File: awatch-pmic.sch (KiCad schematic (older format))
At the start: 14 parts

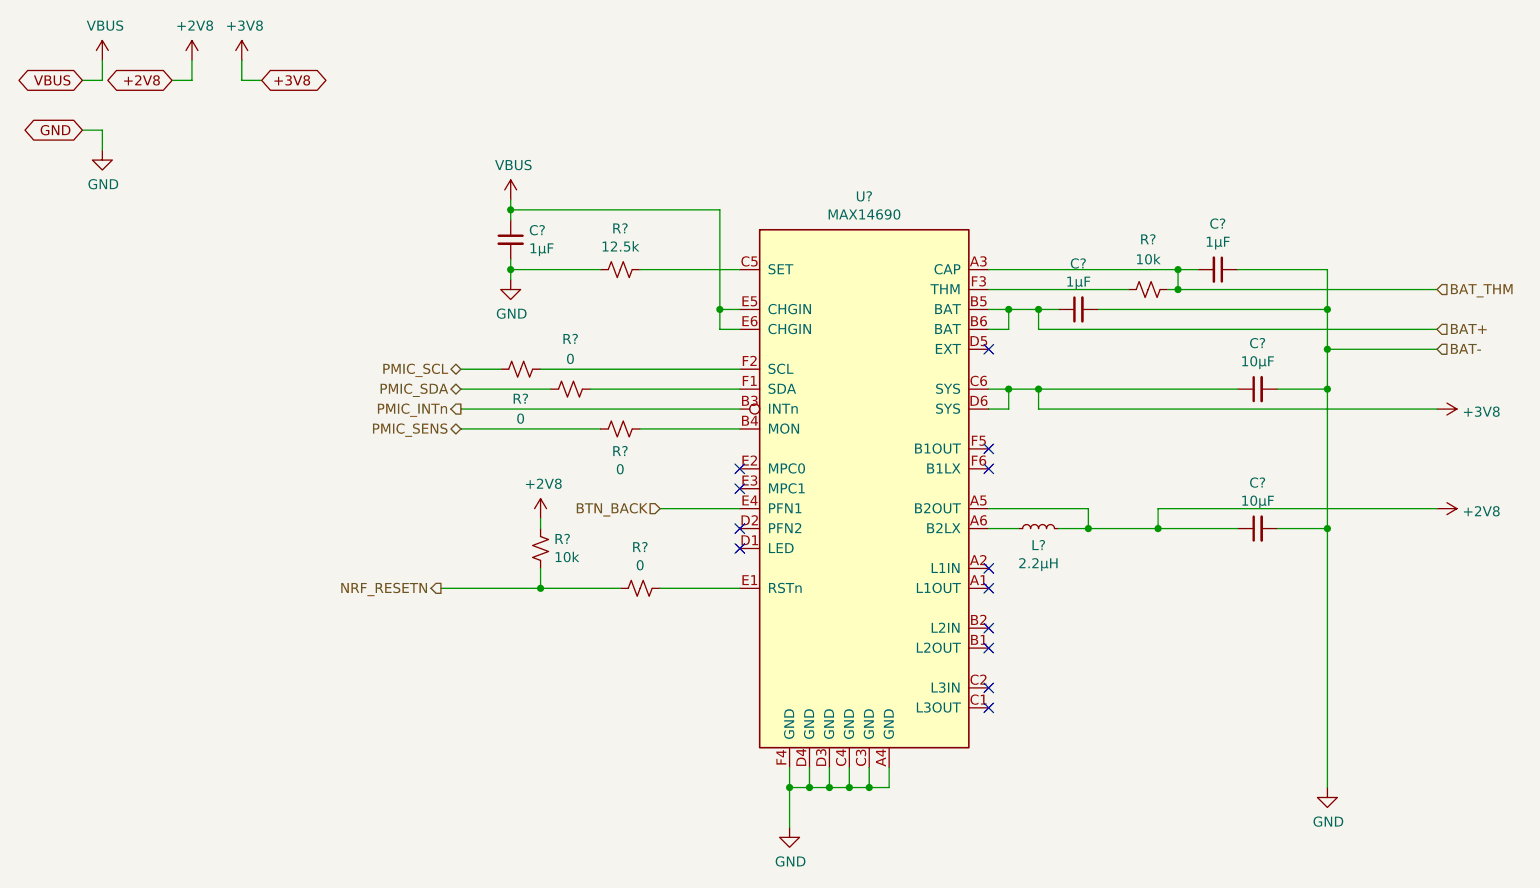
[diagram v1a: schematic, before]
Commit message: Add display.  Add +3.3V LDO for backlight.
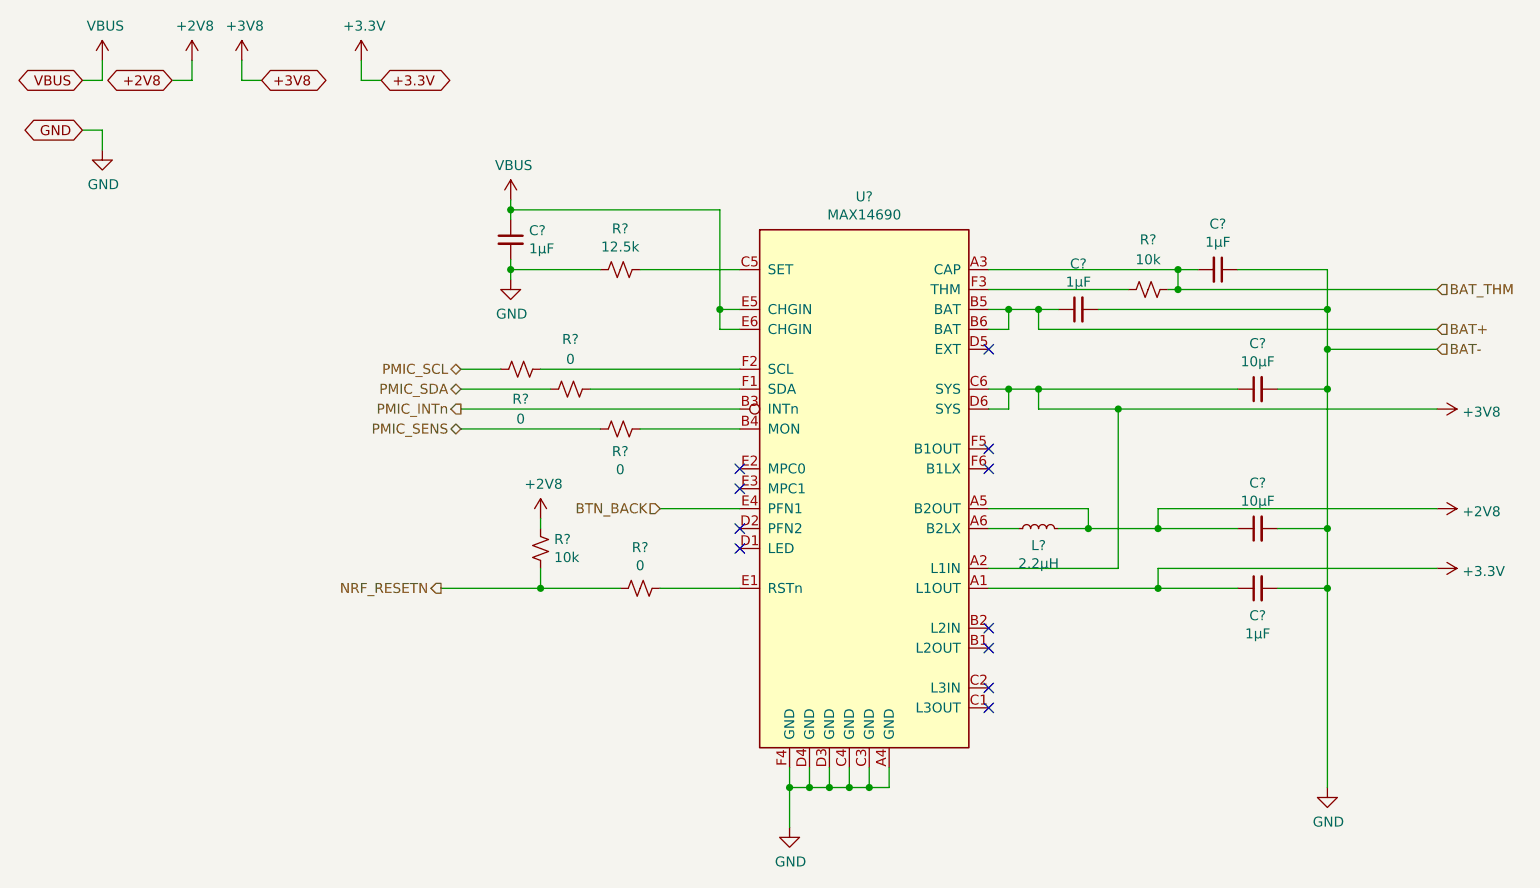
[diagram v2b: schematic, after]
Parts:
- added C?: 1µF, symbol Device:C_Small
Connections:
- net +3V8: now also U?.A2 (L1IN)
- net GND: now also C?.2
- net +3V3: now reaches U?.A1 (L1OUT)
- net +3V3: now also C?.1
- no-connect marks 13 -> 11
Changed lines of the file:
@@
 $Descr A4 11693 8268
 encoding utf-8
-Sheet 3 6
+Sheet 3 7
 Title "AWatch2"
 Date ""
@@
 	6100 2800 6100 2900
 Wire Wire Line
-	6100 2900 8100 2900
+	6100 2900 6500 2900
 Connection ~ 6100 2800
 Wire Wire Line
@@
 Connection ~ 6350 3500
 Wire Wire Line
-	6350 3500 6700 3500
-Wire Wire Line
 	6700 3500 6700 3400
 Wire Wire Line
@@
 	1    0    0    -1
 $EndComp
-NoConn ~ 5850 3700
-NoConn ~ 5850 3800
 NoConn ~ 5850 4000
 NoConn ~ 5850 4100
@@
 Connection ~ 7550 2800
 Wire Wire Line
-	7550 3500 7550 4800
+	7550 3500 7550 3800
 $Comp
 L awatch-parts:MAX14690 U?
@@
 Wire Wire Line
 	3600 3800 3100 3800
+Wire Wire Line
+	6500 3700 5850 3700
+$Comp
+L Device:C_Small C?
+U 1 1 5C4627BE
+P 7200 3800
+F 0 "C?" V 7063 3800 50  0000 C CNN
+F 1 "1µF" V 6972 3800 50  0000 C CNN
+F 2 "" H 7200 3800 50  0001 C CNN
+F 3 "~" H 7200 3800 50  0001 C CNN
+	1    7200 3800
+	0    -1   -1   0
+$EndComp
+Wire Wire Line
+	7100 3800 6700 3800
+Wire Wire Line
+	7300 3800 7550 3800
+Connection ~ 7550 3800
+Wire Wire Line
+	7550 3800 7550 4800
+Wire Wire Line
+	6700 3800 6700 3700
+Wire Wire Line
+	6700 3700 8100 3700
+Connection ~ 6700 3800
+Wire Wire Line
+	6700 3800 5850 3800
+$Comp
+L power:+3.3V #PWR?
+U 1 1 5C469263
+P 8100 3700
+F 0 "#PWR?" H 8100 3550 50  0001 C CNN
+F 1 "+3.3V" V 8115 3828 50  0000 L CNN
+F 2 "" H 8100 3700 50  0001 C CNN
+F 3 "" H 8100 3700 50  0001 C CNN
+	1    8100 3700
+	0    1    1    0
+$EndComp
+Wire Wire Line
+	6350 3500 6700 3500
+Wire Wire Line
+	6500 3700 6500 2900
+Connection ~ 6500 2900
+Wire Wire Line
+	6500 2900 8100 2900
+$Comp
+L power:+3.3V #PWR?
+U 1 1 5C46BDE5
+P 2700 1150
+F 0 "#PWR?" H 2700 1000 50  0001 C CNN
+F 1 "+3.3V" H 2715 1323 50  0000 C CNN
+F 2 "" H 2700 1150 50  0001 C CNN
+F 3 "" H 2700 1150 50  0001 C CNN
+	1    2700 1150
+	1    0    0    -1
+$EndComp
+Text GLabel 2800 1250 2    50   BiDi ~ 0
++3.3V
+Wire Wire Line
+	2800 1250 2700 1250
+Wire Wire Line
+	2700 1250 2700 1150
 $EndSCHEMATC

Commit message: add FTDI
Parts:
- added J?: Conn_01x02, symbol Connector_Generic:Conn_01x02
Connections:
- net BAT_THM: now also R?.2, U?.F3 (THM); no longer C?.2, R?.1, U?.A3 (CAP)
- net VBUS: now also J?.1 (Pin_1); no longer C?.1, U?.E5 (CHGIN), U?.E6 (CHGIN)
- new net: C?.2, R?.1, U?.A3 (CAP)
- new net: C?.1, J?.2 (Pin_2), U?.E5 (CHGIN), U?.E6 (CHGIN)
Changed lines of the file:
@@
 $Descr A4 11693 8268
 encoding utf-8
-Sheet 3 7
+Sheet 3 8
 Title "AWatch2"
 Date ""
@@
 	1    0    0    -1
 $EndComp
-Wire Wire Line
-	3450 1850 3450 1900
 $Comp
 L power:GND #PWR?
@@
 	6800 2200 6900 2200
 Wire Wire Line
-	5850 2300 6550 2300
+	5850 2300 6450 2300
 Wire Wire Line
 	5850 2400 5950 2400
@@
 Wire Wire Line
 	7550 2400 7550 2600
-Wire Wire Line
-	6800 2300 8100 2300
-Connection ~ 6800 2300
-Text HLabel 8100 2300 2    50   Input ~ 0
+Text HLabel 8100 1900 2    50   Input ~ 0
 BAT_THM
 Text HLabel 8100 2500 2    50   Input ~ 0
@@
 L power:VBUS #PWR?
 U 1 1 5C36F827
-P 3450 1850
-F 0 "#PWR?" H 3450 1700 50  0001 C CNN
-F 1 "VBUS" H 3465 2023 50  0000 C CNN
-F 2 "" H 3450 1850 50  0001 C CNN
-F 3 "" H 3450 1850 50  0001 C CNN
-	1    3450 1850
+P 3450 1400
+F 0 "#PWR?" H 3450 1250 50  0001 C CNN
+F 1 "VBUS" H 3465 1573 50  0000 C CNN
+F 2 "" H 3450 1400 50  0001 C CNN
+F 3 "" H 3450 1400 50  0001 C CNN
+	1    3450 1400
 	1    0    0    -1
 $EndComp
@@
 Wire Wire Line
 	2700 1250 2700 1150
+$Comp
+L Connector_Generic:Conn_01x02 J?
+U 1 1 5C478808
+P 3750 1550
+F 0 "J?" H 3830 1542 50  0000 L CNN
+F 1 "Conn_01x02" H 3830 1451 50  0000 L CNN
+F 2 "" H 3750 1550 50  0001 C CNN
+F 3 "~" H 3750 1550 50  0001 C CNN
+	1    3750 1550
+	1    0    0    -1
+$EndComp
+Wire Wire Line
+	3450 1400 3450 1550
+Wire Wire Line
+	3450 1550 3550 1550
+Wire Wire Line
+	3550 1650 3450 1650
+Wire Wire Line
+	3450 1650 3450 1900
+Wire Wire Line
+	6450 2300 6450 1900
+Wire Wire Line
+	6450 1900 8100 1900
+Connection ~ 6450 2300
+Wire Wire Line
+	6450 2300 6550 2300
 $EndSCHEMATC

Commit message: annotate all
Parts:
- gave numbers to parts that had none: 16
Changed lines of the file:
@@
 NRF_RESETN
 $Comp
-L Device:R_Small_US R?
+L Device:R_Small_US R302
 U 1 1 5C35AFEE
 P 3600 3600
-F 0 "R?" H 3532 3554 50  0000 R CNN
+F 0 "R302" H 3532 3554 50  0000 R CNN
 F 1 "10k" H 3532 3645 50  0000 R CNN
 F 2 "" H 3600 3600 50  0001 C CNN
@@
 $EndComp
 $Comp
-L power:+2V8 #PWR?
+L power:+2V8 #PWR0122
 U 1 1 5C35B0A6
 P 3600 3450
-F 0 "#PWR?" H 3600 3300 50  0001 C CNN
+F 0 "#PWR0122" H 3600 3300 50  0001 C CNN
 F 1 "+2V8" H 3615 3623 50  0000 C CNN
 F 2 "" H 3600 3450 50  0001 C CNN
@@
 	4500 2500 4600 2500
 $Comp
-L power:GND #PWR?
+L power:GND #PWR0123
 U 1 1 5C35B422
 P 4850 5000
-F 0 "#PWR?" H 4850 4750 50  0001 C CNN
+F 0 "#PWR0123" H 4850 4750 50  0001 C CNN
 F 1 "GND" H 4855 4827 50  0000 C CNN
 F 2 "" H 4850 5000 50  0001 C CNN
@@
 Connection ~ 5250 4800
 $Comp
-L Device:C_Small C?
+L Device:C_Small C301
 U 1 1 5C35C08D
 P 3450 2050
-F 0 "C?" H 3542 2096 50  0000 L CNN
+F 0 "C301" H 3542 2096 50  0000 L CNN
 F 1 "1µF" H 3542 2005 50  0000 L CNN
 F 2 "" H 3450 2050 50  0001 C CNN
@@
 $EndComp
 $Comp
-L power:GND #PWR?
+L power:GND #PWR0124
 U 1 1 5C35C328
 P 3450 2250
-F 0 "#PWR?" H 3450 2000 50  0001 C CNN
+F 0 "#PWR0124" H 3450 2000 50  0001 C CNN
 F 1 "GND" H 3455 2077 50  0000 C CNN
 F 2 "" H 3450 2250 50  0001 C CNN
@@
 	3450 1900 3450 1950
 $Comp
-L Device:R_Small_US R?
+L Device:R_Small_US R304
 U 1 1 5C35C923
 P 4000 2200
-F 0 "R?" V 3795 2200 50  0000 C CNN
+F 0 "R304" V 3795 2200 50  0000 C CNN
 F 1 "12.5k" V 3886 2200 50  0000 C CNN
 F 2 "" H 4000 2200 50  0001 C CNN
@@
 	3450 2200 3450 2250
 $Comp
-L Device:C_Small C?
+L Device:C_Small C303
 U 1 1 5C35D185
 P 7000 2200
-F 0 "C?" V 6771 2200 50  0000 C CNN
+F 0 "C303" V 6771 2200 50  0000 C CNN
 F 1 "1µF" V 6862 2200 50  0000 C CNN
 F 2 "" H 7000 2200 50  0001 C CNN
@@
 $EndComp
 $Comp
-L power:GND #PWR?
+L power:GND #PWR0125
 U 1 1 5C35D704
 P 7550 4800
-F 0 "#PWR?" H 7550 4550 50  0001 C CNN
+F 0 "#PWR0125" H 7550 4550 50  0001 C CNN
 F 1 "GND" H 7555 4627 50  0000 C CNN
 F 2 "" H 7550 4800 50  0001 C CNN
@@
 $EndComp
 $Comp
-L Device:R_Small_US R?
+L Device:R_Small_US R307
 U 1 1 5C35E21F
 P 6650 2300
-F 0 "R?" V 6400 2300 50  0000 C CNN
+F 0 "R307" V 6400 2300 50  0000 C CNN
 F 1 "10k" V 6500 2300 50  0000 C CNN
 F 2 "" H 6650 2300 50  0001 C CNN
@@
 NoConn ~ 5850 2600
 $Comp
-L Device:C_Small C?
+L Device:C_Small C302
 U 1 1 5C360727
 P 6300 2400
-F 0 "C?" V 6529 2400 50  0000 C CNN
+F 0 "C302" V 6529 2400 50  0000 C CNN
 F 1 "1µF" V 6438 2400 50  0000 C CNN
 F 2 "" H 6300 2400 50  0001 C CNN
@@
 	5950 2900 5850 2900
 $Comp
-L Device:C_Small C?
+L Device:C_Small C304
 U 1 1 5C3661E5
 P 7200 2800
-F 0 "C?" V 7429 2800 50  0000 C CNN
+F 0 "C304" V 7429 2800 50  0000 C CNN
 F 1 "10µF" V 7338 2800 50  0000 C CNN
 F 2 "" H 7200 2800 50  0001 C CNN
@@
 	7300 2800 7550 2800
 $Comp
-L power:+3V8 #PWR?
+L power:+3V8 #PWR0126
 U 1 1 5C368771
 P 8100 2900
-F 0 "#PWR?" H 8100 2750 50  0001 C CNN
+F 0 "#PWR0126" H 8100 2750 50  0001 C CNN
 F 1 "+3V8" V 8115 3028 50  0000 L CNN
 F 2 "" H 8100 2900 50  0001 C CNN
@@
 	6100 2800 7100 2800
 $Comp
-L Device:L_Small L?
+L Device:L_Small L301
 U 1 1 5C36A501
 P 6100 3500
-F 0 "L?" V 6015 3500 50  0000 C CNN
+F 0 "L301" V 6015 3500 50  0000 C CNN
 F 1 "2.2µH" V 5924 3500 50  0000 C CNN
 F 2 "" H 6100 3500 50  0001 C CNN
@@
 	6000 3500 5850 3500
 $Comp
-L Device:C_Small C?
+L Device:C_Small C305
 U 1 1 5C36B423
 P 7200 3500
-F 0 "C?" V 7429 3500 50  0000 C CNN
+F 0 "C305" V 7429 3500 50  0000 C CNN
 F 1 "10µF" V 7338 3500 50  0000 C CNN
 F 2 "" H 7200 3500 50  0001 C CNN
@@
 	6700 3500 7100 3500
 $Comp
-L power:+2V8 #PWR?
+L power:+2V8 #PWR0127
 U 1 1 5C36F775
 P 8100 3400
-F 0 "#PWR?" H 8100 3250 50  0001 C CNN
+F 0 "#PWR0127" H 8100 3250 50  0001 C CNN
 F 1 "+2V8" V 8115 3528 50  0000 L CNN
 F 2 "" H 8100 3400 50  0001 C CNN
@@
 $EndComp
 $Comp
-L power:VBUS #PWR?
+L power:VBUS #PWR0128
 U 1 1 5C36F827
 P 3450 1400
-F 0 "#PWR?" H 3450 1250 50  0001 C CNN
+F 0 "#PWR0128" H 3450 1250 50  0001 C CNN
 F 1 "VBUS" H 3465 1573 50  0000 C CNN
 F 2 "" H 3450 1400 50  0001 C CNN
@@
 	7550 3500 7550 3800
 $Comp
-L awatch-parts:MAX14690 U?
+L awatch-parts:MAX14690 U301
 U 1 1 5C35AD5E
 P 4700 2000
-F 0 "U?" H 5225 2166 50  0000 C CNN
+F 0 "U301" H 5225 2166 50  0000 C CNN
 F 1 "MAX14690" H 5225 2075 50  0000 C CNN
 F 2 "" H 4700 2000 50  0001 C CNN
@@
 PMIC_INTn
 $Comp
-L power:VBUS #PWR?
+L power:VBUS #PWR0129
 U 1 1 5C387312
 P 1400 1150
-F 0 "#PWR?" H 1400 1000 50  0001 C CNN
+F 0 "#PWR0129" H 1400 1000 50  0001 C CNN
 F 1 "VBUS" H 1415 1323 50  0000 C CNN
 F 2 "" H 1400 1150 50  0001 C CNN
@@
 	1400 1250 1300 1250
 $Comp
-L power:+2V8 #PWR?
+L power:+2V8 #PWR0130
 U 1 1 5C388978
 P 1850 1150
-F 0 "#PWR?" H 1850 1000 50  0001 C CNN
+F 0 "#PWR0130" H 1850 1000 50  0001 C CNN
 F 1 "+2V8" H 1865 1323 50  0000 C CNN
 F 2 "" H 1850 1150 50  0001 C CNN
@@
 $EndComp
 $Comp
-L power:+3V8 #PWR?
+L power:+3V8 #PWR0131
 U 1 1 5C3889BF
 P 2100 1150
-F 0 "#PWR?" H 2100 1000 50  0001 C CNN
+F 0 "#PWR0131" H 2100 1000 50  0001 C CNN
 F 1 "+3V8" H 2115 1323 50  0000 C CNN
 F 2 "" H 2100 1150 50  0001 C CNN
@@
 $EndComp
 $Comp
-L power:GND #PWR?
+L power:GND #PWR0132
 U 1 1 5C388A38
 P 1400 1600
-F 0 "#PWR?" H 1400 1350 50  0001 C CNN
+F 0 "#PWR0132" H 1400 1350 50  0001 C CNN
 F 1 "GND" H 1405 1427 50  0000 C CNN
 F 2 "" H 1400 1600 50  0001 C CNN
@@
 	2100 1250 2200 1250
 $Comp
-L Device:R_Small_US R?
+L Device:R_Small_US R306
 U 1 1 5C39F6F8
 P 4100 3800
-F 0 "R?" V 3895 3800 50  0000 C CNN
+F 0 "R306" V 3895 3800 50  0000 C CNN
 F 1 "0" V 3986 3800 50  0000 C CNN
 F 2 "" H 4100 3800 50  0001 C CNN
@@
 Connection ~ 4500 2400
 $Comp
-L Device:R_Small_US R?
+L Device:R_Small_US R301
 U 1 1 5C3AA357
 P 3500 2700
-F 0 "R?" V 3650 2700 50  0000 C CNN
+F 0 "R301" V 3650 2700 50  0000 C CNN
 F 1 "0" V 3750 2700 50  0000 C CNN
 F 2 "" H 3500 2700 50  0001 C CNN
@@
 $EndComp
 $Comp
-L Device:R_Small_US R?
+L Device:R_Small_US R303
 U 1 1 5C3AA38D
 P 3750 2800
-F 0 "R?" V 3500 2800 50  0000 C CNN
+F 0 "R303" V 3500 2800 50  0000 C CNN
 F 1 "0" V 3600 2800 50  0000 C CNN
 F 2 "" H 3750 2800 50  0001 C CNN
@@
 	3200 2900 4600 2900
 $Comp
-L Device:R_Small_US R?
+L Device:R_Small_US R305
 U 1 1 5C3B594C
 P 4000 3000
-F 0 "R?" V 4113 3000 50  0000 C CNN
+F 0 "R305" V 4113 3000 50  0000 C CNN
 F 1 "0" V 4204 3000 50  0000 C CNN
 F 2 "" H 4000 3000 50  0001 C CNN
@@
 	6500 3700 5850 3700
 $Comp
-L Device:C_Small C?
+L Device:C_Small C306
 U 1 1 5C4627BE
 P 7200 3800
-F 0 "C?" V 7063 3800 50  0000 C CNN
+F 0 "C306" V 7063 3800 50  0000 C CNN
 F 1 "1µF" V 6972 3800 50  0000 C CNN
 F 2 "" H 7200 3800 50  0001 C CNN
@@
 	6700 3800 5850 3800
 $Comp
-L power:+3.3V #PWR?
+L power:+3.3V #PWR0133
 U 1 1 5C469263
 P 8100 3700
-F 0 "#PWR?" H 8100 3550 50  0001 C CNN
+F 0 "#PWR0133" H 8100 3550 50  0001 C CNN
 F 1 "+3.3V" V 8115 3828 50  0000 L CNN
 F 2 "" H 8100 3700 50  0001 C CNN
@@
 	6500 2900 8100 2900
 $Comp
-L power:+3.3V #PWR?
+L power:+3.3V #PWR0134
 U 1 1 5C46BDE5
 P 2700 1150
-F 0 "#PWR?" H 2700 1000 50  0001 C CNN
+F 0 "#PWR0134" H 2700 1000 50  0001 C CNN
 F 1 "+3.3V" H 2715 1323 50  0000 C CNN
 F 2 "" H 2700 1150 50  0001 C CNN
@@
 	2700 1250 2700 1150
 $Comp
-L Connector_Generic:Conn_01x02 J?
+L Connector_Generic:Conn_01x02 J301
 U 1 1 5C478808
 P 3750 1550
-F 0 "J?" H 3830 1542 50  0000 L CNN
+F 0 "J301" H 3830 1542 50  0000 L CNN
 F 1 "Conn_01x02" H 3830 1451 50  0000 L CNN
 F 2 "" H 3750 1550 50  0001 C CNN
